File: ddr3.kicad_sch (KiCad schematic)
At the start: 36 parts, among them U10 AS4C256M16D3, U11 TPS51200DRC

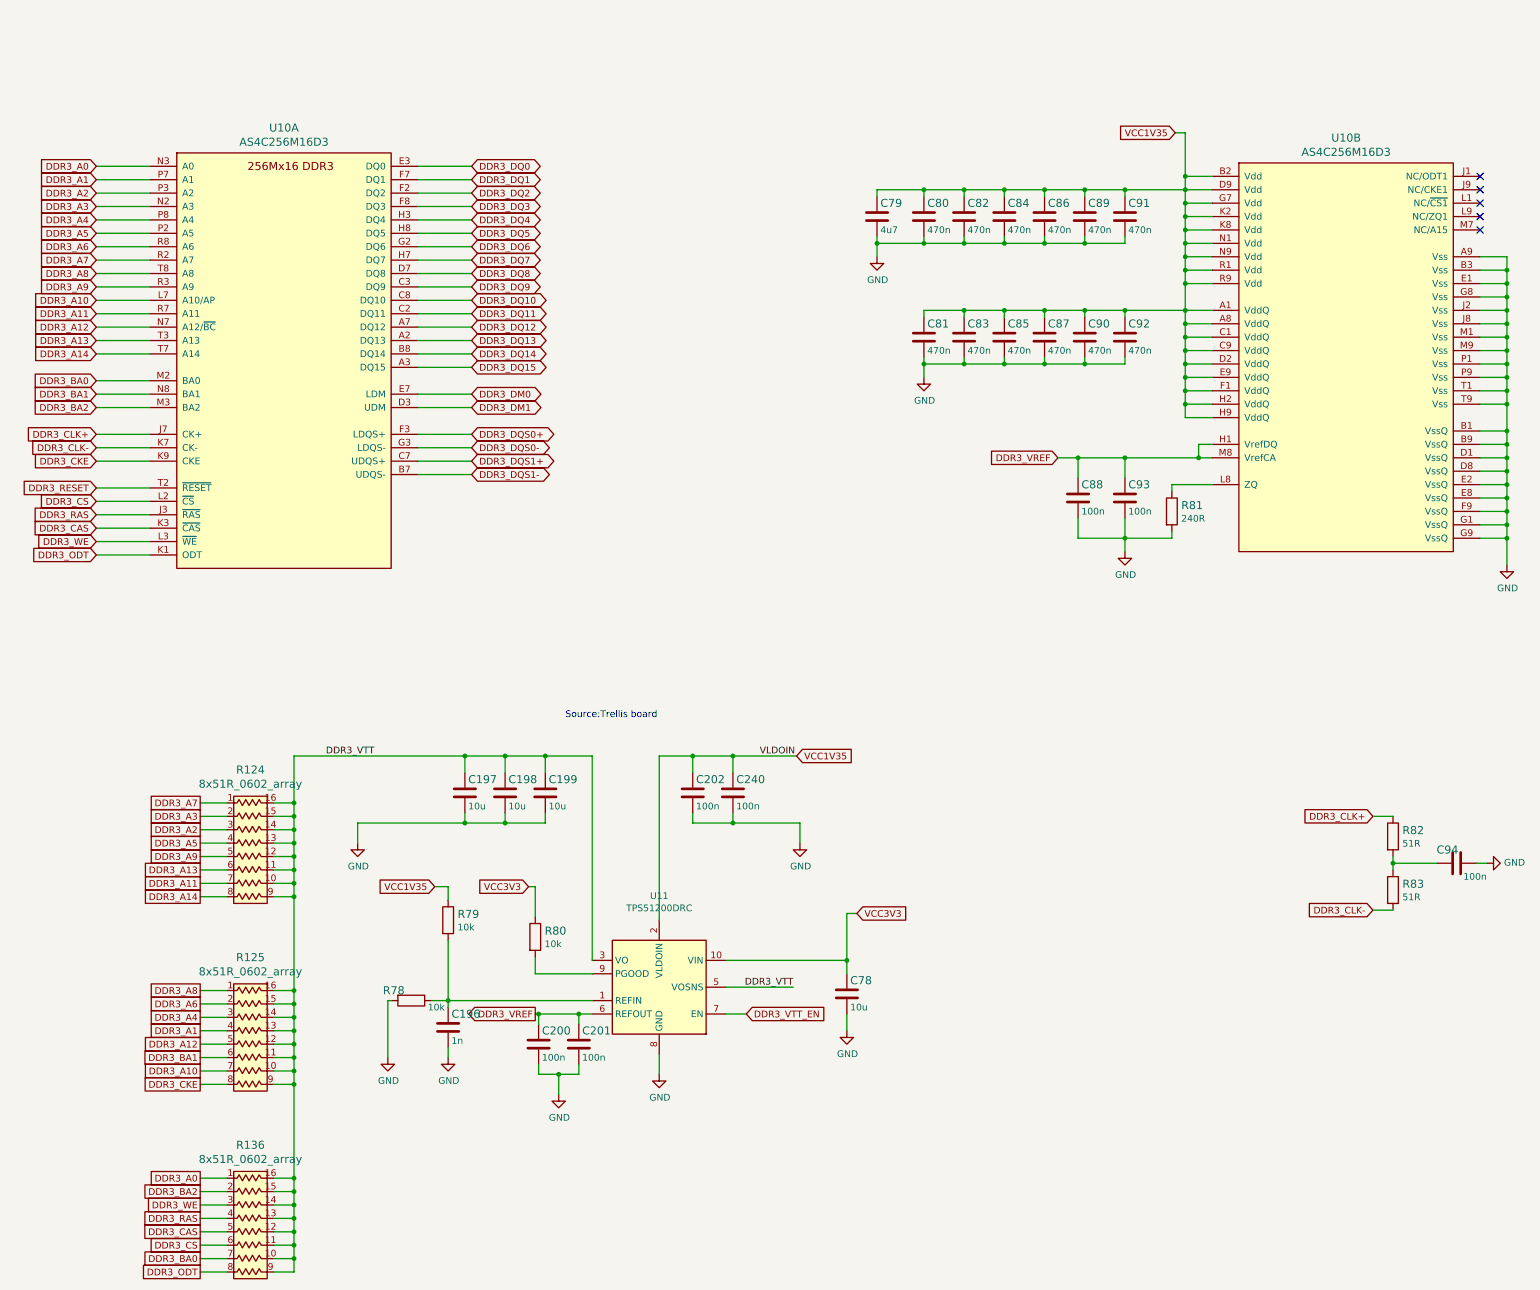
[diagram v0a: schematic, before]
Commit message: [#61392] Convert project to KiCad 7
[#61392] Run globlib

[#61392] Allign components to the grid

[#61392] Update oshw and antmicro logo

[#61392] Standarize ethernet sheet

[#61392] Standarize pcie-conn sheet

[#61392] Standarize rot sheet

[#61392] Standarize edge-connector sheet

[#61392] WIP:Standarize interfaces sheet

[#61392] WIP: Route interfaces sheet

[#61392] Finish standarizing interfaces sheet

[#61392] Update interfaces sheet with fixed 2N7002

[#61392] WIP:Standarize ddr3 sheet

[#61392] Standarize ddr3 sheet

[#61392] Standarize power-supply sheet

[#61392] Standarize fpga power-supply sheet

[#61392] Remove TODO comments from power-banks sheet

[#61392] Standarize fpga-banks sheet

[#61392] Ignore Input pins not driven ERC

[#61392] Clear off grid ERCs

[#61392] Exclude ERC DDR3_VTT_EN NC

[#61392] Bump rev to 1.2.1

[#61392] Bump PCB rev to 1.2.1
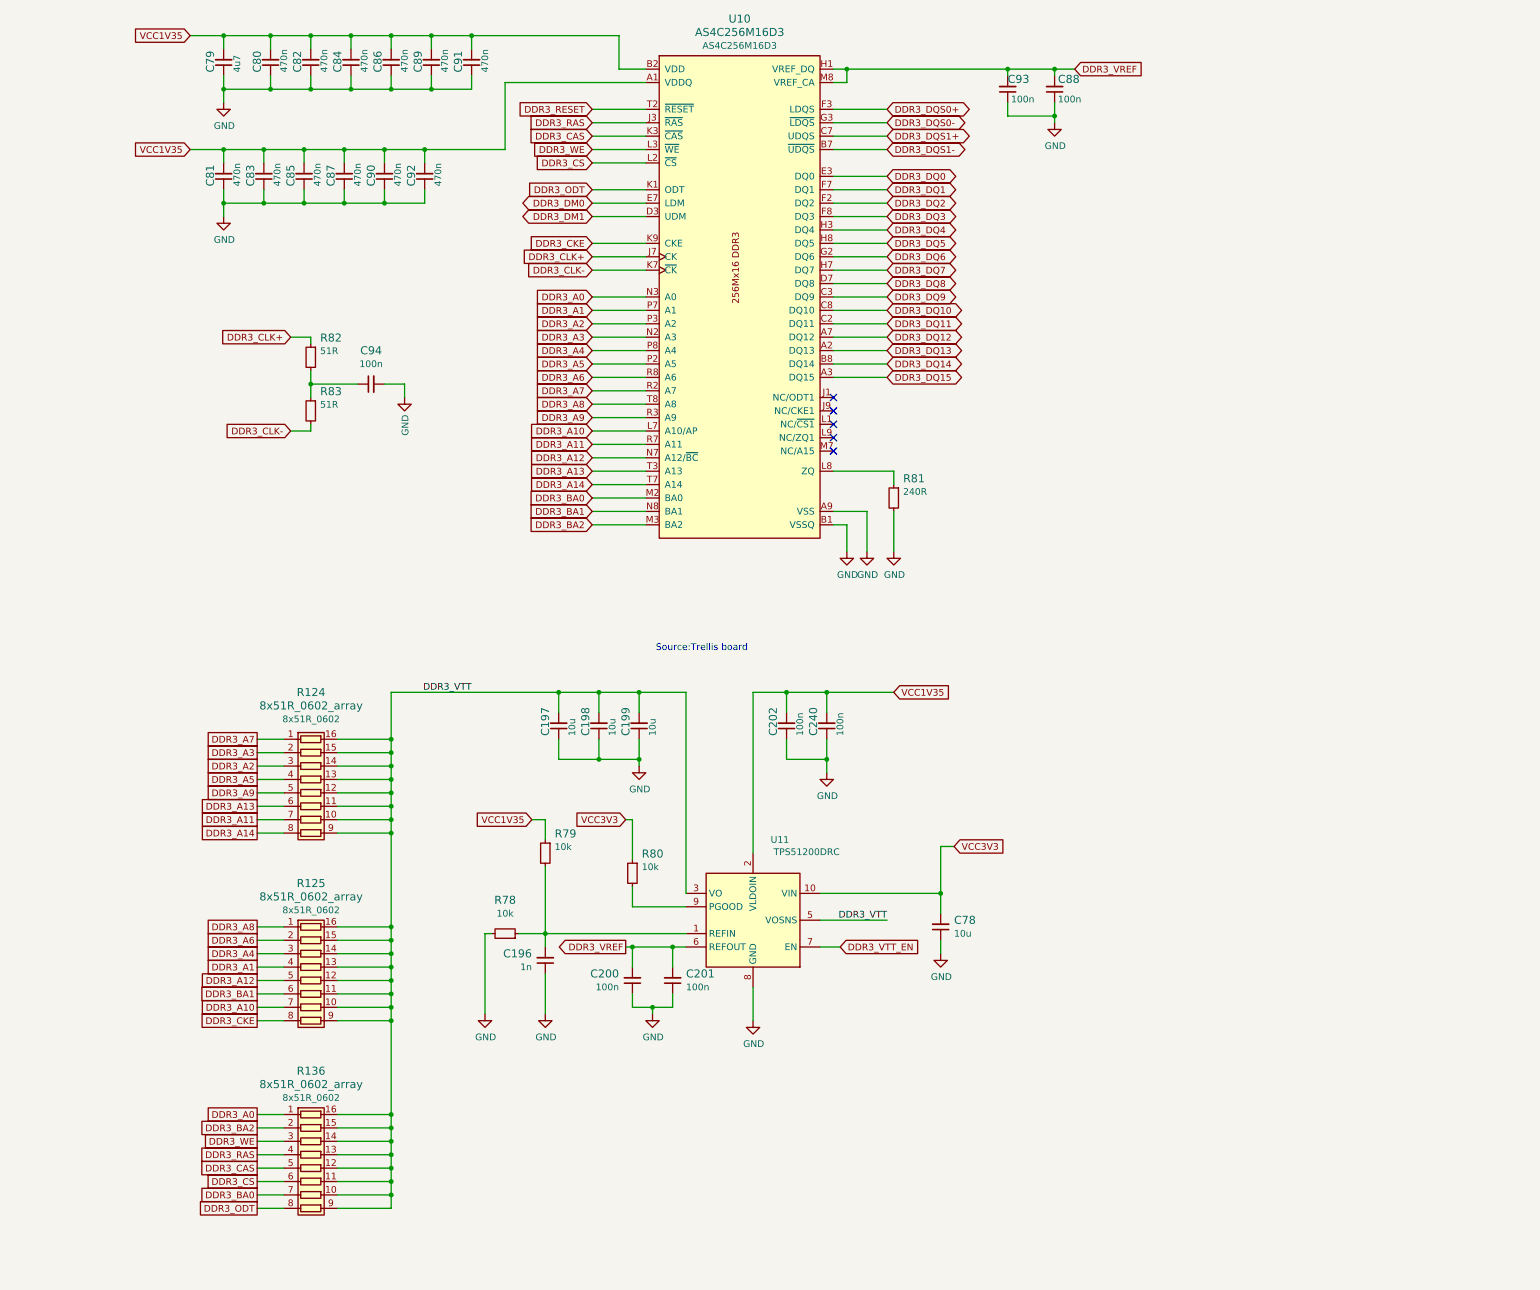
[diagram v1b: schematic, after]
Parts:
- removed unit 2 of U10
- C196: footprint ecp5-dc-scm-footprints:0402-res -> antmicro-footprints:C_0402_1005Metric; symbol ecp5-dc-scm:C_1n_0402 -> antmicroCapacitors0402:C_1n_0402; Author (none) -> Antmicro; Dielectric (none) -> C0G; License (none) -> Apache-2.0; MPN CC0402KRX7R9BB102 -> GRM1555C1H102JA01D; Manufacturer YAGEO -> Murata; Public (none) -> False; Voltage (none) -> 50V
- C197, C198, C199, C78: footprint ecp5-dc-scm-footprints:0402-cap -> antmicro-footprints:C_0402_1005Metric; symbol ecp5-dc-scm:C_10u_0402 -> antmicroCapacitors0402:C_10u_0402; Author (none) -> Antmicro; License (none) -> Apache-2.0; MPN GRM155R60J106ME44D -> CC0402MRX5R5BB106; Manufacturer MURATA -> YAGEO; Public (none) -> False
- C200, C201, C202, C240, C88, C93, C94: footprint ecp5-dc-scm-footprints:0402-cap -> antmicro-footprints:C_0402_1005Metric; symbol ecp5-dc-scm:C_100n_0402 -> antmicroCapacitors0402:C_100n_0402; Author (none) -> Antmicro; Dielectric (none) -> X5R; License (none) -> Apache-2.0; MPN 0402X104K6R3CT -> GRM155R61H104KE14D; Manufacturer Walsin -> Murata; Public (none) -> False; Voltage (none) -> 50V
- C79: footprint ecp5-dc-scm-footprints:0402-cap -> antmicro-footprints:C_0402_1005Metric; symbol ecp5-dc-scm:C_4u7_0402 -> antmicroCapacitors0402:C_4u7_0402; Author (none) -> Antmicro; License (none) -> Apache-2.0; Manufacturer MURATA -> Murata; Public (none) -> False
- C80, C81, C82, C83, C84, C85, C86, C87, C89, C90, C91, C92: footprint ecp5-dc-scm-footprints:0402-cap -> antmicro-footprints:C_0402_1005Metric; symbol ecp5-dc-scm:C_470n_0402 -> antmicroCapacitors0402:C_470n_0402; Author (none) -> Antmicro; License (none) -> Apache-2.0; Public (none) -> False
- R124, R125, R136: footprint ecp5-dc-scm-footprints:R_Array_Convex_8x0602 -> antmicro-footprints:R_Array_8x0602_Panasonic_EXB2HV; symbol ecp5-dc-scm:8x51R_0602_array -> antmicroResistorNetworksArrays:8x51R_0602_array; Author (none) -> Antmicro; License (none) -> Apache-2.0; Val (none) -> 8x51R_0602
- R78, R79, R80: footprint ecp5-dc-scm-footprints:0402-res -> antmicro-footprints:R_0402_1005Metric; symbol ecp5-dc-scm:R_10k_0402 -> antmicroResistors0402:R_10k_0402; Author (none) -> Antmicro; License (none) -> Apache-2.0; MPN CRCW040210K0FKEDHP -> CR0402-FX-1002GLF; Manufacturer VISHAY -> Bourns; Public (none) -> False; Tolerance (none) -> 1%
- R81: footprint ecp5-dc-scm-footprints:0402-res -> antmicro-footprints:R_0402_1005Metric; symbol ecp5-dc-scm:R_240R_0402 -> antmicroResistors0402:R_240R_0402; Author (none) -> Antmicro; License (none) -> Apache-2.0; MPN ERJ2GEJ241X -> CR0402-FX-2400GLF; Manufacturer PANASONIC -> Bourns; Public (none) -> False; Tolerance (none) -> 1%
- R82, R83: footprint ecp5-dc-scm-footprints:0402-res -> antmicro-footprints:R_0402_1005Metric; symbol ecp5-dc-scm:R_51R_0402 -> antmicroResistors0402:R_51R_0402; Author (none) -> Antmicro; License (none) -> Apache-2.0; MPN RC0402FR-0751RL -> CR0402-FX-51R0GLF; Manufacturer YAGEO -> Bourns; Public (none) -> False; Tolerance (none) -> 1%
- U10: footprint ecp5-dc-scm-footprints:BGA-96_9.0x13.0mm_Layout2x3x16_P0.8mm -> antmicro-footprints:BGA-96_9.0x13.0mm_Layout2x3x16_P0.8mm; symbol ecp5-dc-scm:AS4C256M16D3 -> antmicroMemory:AS4C256M16D3; Author (none) -> Antmicro; License (none) -> Apache-2.0; MPN (none) -> AS4C256M16D3; Manufacturer (none) -> Alliance Memory
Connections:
- net DDR3_VREF: now also C200.2, C201.2, C88.2, C93.2, U10.H1 (VREF_DQ), U10.M8 (VREF_CA); no longer C200.1, C201.1, C88.1, C93.1
- net DDR3_VTT: now also C197.2, C198.2, C199.2; no longer C197.1, C198.1, C199.1
- net GND: now also C196.1, C197.1, C198.1, C199.1, C200.1, C201.1, C202.1, C240.1, C78.1, C79.1, C80.1, C81.1, C82.1, C83.1, C84.1, C85.1, C86.1, C87.1, C88.1, C89.1, C90.1, C91.1, C92.1, C93.1, C94.2, U10.A9 (VSS), U10.B1 (VSSQ), U10.B3 (VSS), U10.B9 (VSSQ), U10.D1 (VSSQ), U10.D8 (VSSQ), U10.E1 (VSS), U10.E2 (VSSQ), U10.E8 (VSSQ), U10.F9 (VSSQ), U10.G1 (VSSQ), U10.G8 (VSS), U10.G9 (VSSQ), U10.J2 (VSS), U10.J8 (VSS), U10.M1 (VSS), U10.M9 (VSS), U10.P1 (VSS), U10.P9 (VSS), U10.T1 (VSS), U10.T9 (VSS); no longer C196.2, C197.2, C198.2, C199.2, C200.2, C201.2, C202.2, C240.2, C78.2, C79.2, C80.2, C81.2, C82.2, C83.2, C84.2, C85.2, C86.2, C87.2, C88.2, C89.2, C90.2, C91.2, C92.2, C93.2, C94.1
- net VCC1V35: now also C202.2, C240.2, C79.2, C80.2, C81.2, C82.2, C83.2, C84.2, C85.2, C86.2, C87.2, C89.2, C90.2, C91.2, C92.2, U10.A1 (VDDQ), U10.A8 (VDDQ), U10.B2 (VDD), U10.C1 (VDDQ), U10.C9 (VDDQ), U10.D2 (VDDQ), U10.D9 (VDD), U10.E9 (VDDQ), U10.F1 (VDDQ), U10.G7 (VDD), U10.H2 (VDDQ), U10.H9 (VDDQ), U10.K2 (VDD), U10.K8 (VDD), U10.N1 (VDD), U10.N9 (VDD), U10.R1 (VDD), U10.R9 (VDD); no longer C202.1, C240.1, C79.1, C80.1, C81.1, C82.1, C83.1, C84.1, C85.1, C86.1, C87.1, C89.1, C90.1, C91.1, C92.1
- net VCC3V3: now also C78.2; no longer C78.1
- net at R82.2, R83.1: now also C94.1; no longer C94.2
- net at R81.1: now also U10.L8 (ZQ)
- net at R78.1, R79.2, U11.1 (REFIN): now also C196.2; no longer C196.1
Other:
- moved on the sheet: C196, C197, C198, C199, C200, C201, C202, C240, C78, C79, C80, C81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

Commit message: [#61392] Import changes to the PCB
[#61392] Fix D2 orientation

[#61392] Fix J2 J1 D6 orientation

[#61392] WIP: PCB Fix caps orienations

[#61392] PCB Fix caps orienations

[#61392] Fix missalligned edge cuts

[#61392] Sync Sch with PCB

[#61392] Fix silk clipped by edge cuts

[#61392] Ignore TP no courtyard drc

[#61392] Update C_0603 footprints

[#61392] Update R_0402 footprints

[#61392] Update Sot-23 footprints

[#61392] Update QFN and IHLP footprints

[#61392] Update remaining footprints

[#61392] Change minimal text height to 0.7mm

[#61392] Clear remaining Silk DRCs

[#61392] Update TPS51200DRCT symbol

[#61392] Update 9774040151

[#61392] Update W25Q32JVS

[#61392] Update ECS-3225MVQ-1000CN-TR

[#61392] Clean ERC

[#61392] Remove obsolete files

[#61392] Synhronize components with library

[#61392] Remove globlib leftovers

[#61392] Synchronize components with libraries (WiP)

[#61392] Clean ERC and DRC

[#61392] Set J5 to DNP

[#61392] Add PCB SHA string, update layer names

[#61392] Update assets

[#62567] Add stackup.csv

[#62567] Input elecric constants for the board stackup

[#62567] Update stackup.csv
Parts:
- removed U11: TPS51200DRC, ecp5-dc-scm-footprints:VSON-10-1EP_3x3mm, symbol ecp5-dc-scm:TPS51200DRC
- added U11: TPS51200DRCT, antmicro-footprints:VSON-10-1EP_3x3mm, symbol antmicroPMICVoltageRegulatorsDCDCSwitchingControllers:TPS51200DRCT
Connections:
- net DDR3_VREF: now also U11.6 (REFOUT)
- net DDR3_VTT: now also U11.3 (VO), U11.5 (VOSNS)
- net DDR3_VTT_EN: now also U11.7 (EN)
- net GND: now also U11.11 (GND), U11.4 (GND), U11.8 (GND)
- net VCC1V35: now also U11.2 (VLDOIN)
- net VCC3V3: now also U11.10 (VIN)
- net at C196.2, R78.1, R79.2: now also U11.1 (REFIN)
- net at R80.2: now also U11.9 (PGOOD)
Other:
- moved on the sheet: C196, C200, C201, C202, C240, C78, R78, R79, R80
